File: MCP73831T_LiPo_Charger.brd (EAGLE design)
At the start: 12.7 x 24.1 mm, 10 parts, among them U4 MCP73831

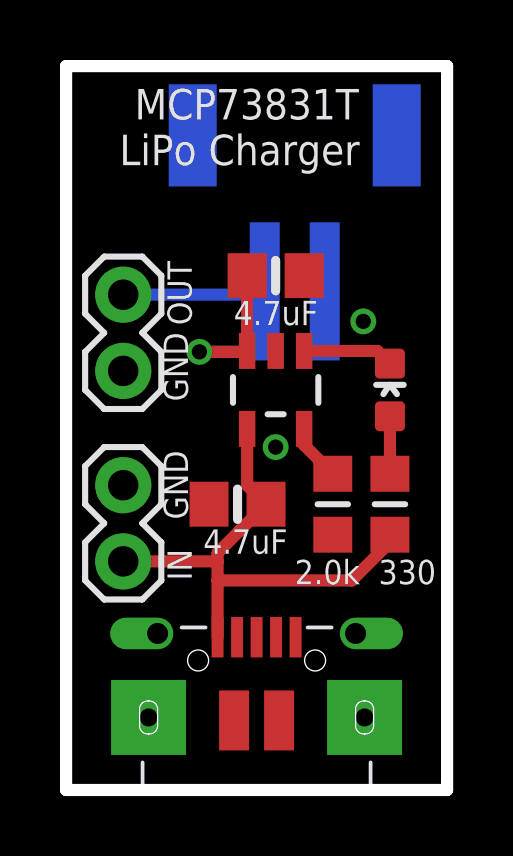
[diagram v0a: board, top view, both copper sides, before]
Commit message: modified microUSB port
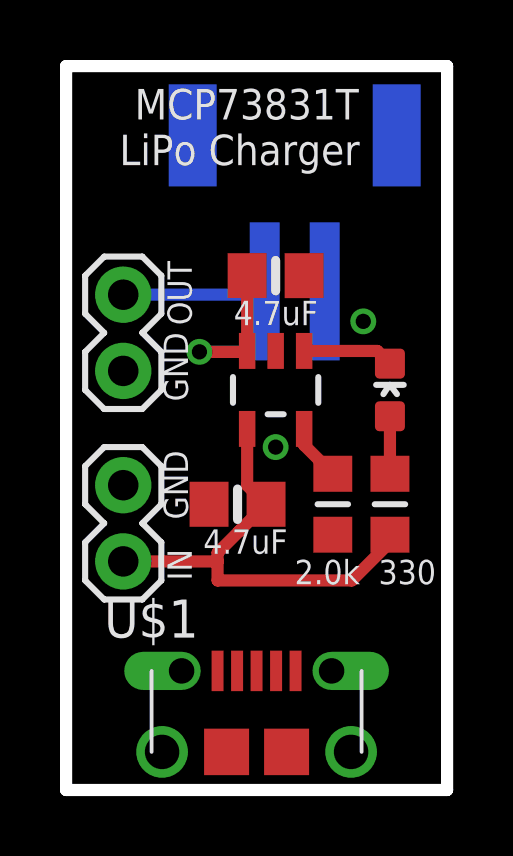
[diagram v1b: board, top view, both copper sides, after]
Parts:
- removed X1: (no value), microbuilder:4UCONN_20329
- added U$1: AMPHENOL_MICROUSB, sharkdunio:AMPHENOL_MICROUSB
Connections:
- net GND: now also U$1.2, U$1.3, U$1.4, U$1.5; no longer X1.BASE@1, X1.BASE@2, X1.GND, X1.SPRT@1, X1.SPRT@2, X1.SPRT@3, X1.SPRT@4
- net VIN: now also U$1.1; no longer X1.VBUS
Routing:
- net VIN: track 17.5 -> 15.6 mm
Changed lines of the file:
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@@
 <attribute name="VALUE" x="7.9375" y="13.5255" size="0.4064" layer="27" rot="R180"/>
 </element>
-<element name="X1" library="microbuilder" package="4UCONN_20329" value="" x="6.35" y="4.318" smashed="yes">
-<attribute name="VALUE" x="3.572" y="-2.092" size="0.4064" layer="27" ratio="10"/>
-</element>
+<element name="U$1" library="sharkdunio" package="AMPHENOL_MICROUSB" value="AMPHENOL_MICROUSB" x="6.35" y="1.27"/>
 </elements>
 <signals>
@@
 <contactref element="U4" pad="2"/>
 <contactref element="R8" pad="1"/>
-<contactref element="X1" pad="BASE@1"/>
-<contactref element="X1" pad="BASE@2"/>
-<contactref element="X1" pad="GND"/>
-<contactref element="X1" pad="SPRT@1"/>
-<contactref element="X1" pad="SPRT@2"/>
-<contactref element="X1" pad="SPRT@3"/>
-<contactref element="X1" pad="SPRT@4"/>
 <contactref element="JP1" pad="1"/>
 <contactref element="J1" pad="1"/>
@@
 <via x="6.985" y="11.43" extent="1-16" drill="0.508"/>
 <via x="9.906" y="15.621" extent="1-16" drill="0.508"/>
+<contactref element="U$1" pad="5"/>
+<contactref element="U$1" pad="4"/>
+<contactref element="U$1" pad="2"/>
+<contactref element="U$1" pad="3"/>
+<wire x1="8.62" y1="16.62" x2="7.935" y2="17.145" width="0" layer="19" extent="1-16"/>
+<wire x1="9.906" y1="15.621" x2="8.62" y2="16.62" width="0" layer="19" extent="16-16"/>
+<wire x1="6.985" y1="14.6351" x2="8.62" y2="16.62" width="0" layer="19" extent="1-16"/>
+<wire x1="6.985" y1="11.43" x2="6.985" y2="14.6351" width="0" layer="19" extent="1-1"/>
+<wire x1="4.765" y1="9.525" x2="6.985" y2="11.43" width="0" layer="19" extent="1-1"/>
+<wire x1="1.905" y1="10.16" x2="4.765" y2="9.525" width="0" layer="19" extent="1-1"/>
+<wire x1="8.89" y1="8.509" x2="6.985" y2="11.43" width="0" layer="19" extent="1-1"/>
+<wire x1="1.905" y1="13.97" x2="1.905" y2="10.16" width="0" layer="19" extent="1-1"/>
+<wire x1="7.65" y1="3.97" x2="8.89" y2="8.509" width="0" layer="19" extent="1-1"/>
+<wire x1="7" y1="3.97" x2="7.65" y2="3.97" width="0" layer="19" extent="1-1"/>
+<wire x1="6.35" y1="3.97" x2="7" y2="3.97" width="0" layer="19" extent="1-1"/>
+<wire x1="5.7" y1="3.97" x2="6.35" y2="3.97" width="0" layer="19" extent="1-1"/>
 </signal>
 <signal name="V_RAW">
@@
 <contactref element="R7" pad="1"/>
 <contactref element="C7" pad="1"/>
-<contactref element="X1" pad="VBUS"/>
 <contactref element="J1" pad="2"/>
 <wire x1="6.035" y1="12.0349" x2="6.035" y2="10.155" width="0.4064" layer="1"/>
@@
 <wire x1="5.7706" y1="8.62770625" x2="5.7706" y2="8.6306" width="0.4064" layer="1"/>
 <wire x1="5.7706" y1="8.6306" x2="6.665" y2="9.525" width="0.4064" layer="1"/>
-<wire x1="5.05" y1="6.985" x2="5.05" y2="5.093" width="0.4064" layer="1"/>
 <wire x1="5.05" y1="6.985" x2="5.05" y2="7.62" width="0.4064" layer="1"/>
 <wire x1="5.05" y1="7.62" x2="5.05" y2="7.90710625" width="0.4064" layer="1"/>
@@
 <wire x1="10.795" y1="8.255" x2="9.525" y2="6.985" width="0.4064" layer="1"/>
 <wire x1="9.525" y1="6.985" x2="5.05" y2="6.985" width="0.4064" layer="1"/>
+<contactref element="U$1" pad="1"/>
+<wire x1="5.05" y1="3.97" x2="5.05" y2="6.985" width="0" layer="19" extent="1-1"/>
 </signal>
 </signals>

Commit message: modified microusb port and lipo schematic
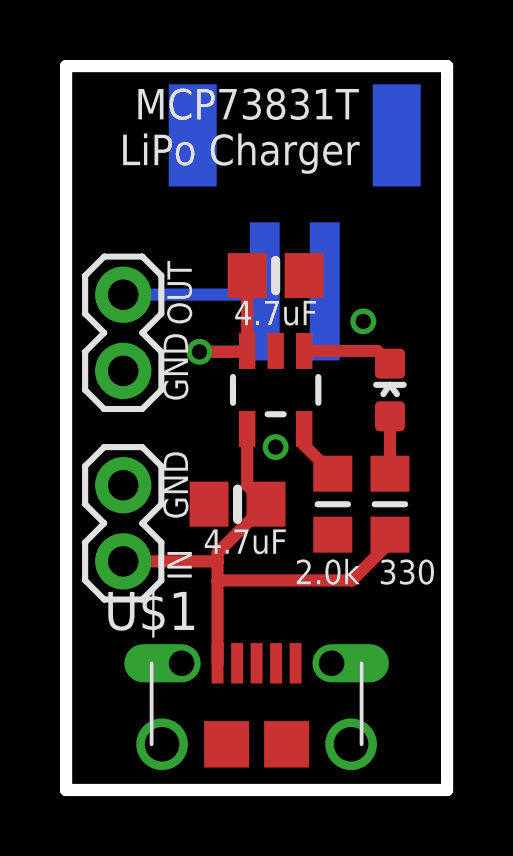
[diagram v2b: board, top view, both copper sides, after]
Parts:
- moved U$1 0.25 mm to (6.35, 1.52)
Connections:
- net GND: now also U$1.10, U$1.11, U$1.6, U$1.7, U$1.8, U$1.9; no longer U$1.2, U$1.3, U$1.4
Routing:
- net VIN: track 15.6 -> 18.4 mm
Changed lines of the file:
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@@
 <attribute name="VALUE" x="7.9375" y="13.5255" size="0.4064" layer="27" rot="R180"/>
 </element>
-<element name="U$1" library="sharkdunio" package="AMPHENOL_MICROUSB" value="AMPHENOL_MICROUSB" x="6.35" y="1.27"/>
+<element name="U$1" library="sharkdunio" package="AMPHENOL_MICROUSB" value="AMPHENOL_MICROUSB" x="6.35" y="1.524"/>
 </elements>
 <signals>
@@
 <via x="6.985" y="11.43" extent="1-16" drill="0.508"/>
 <via x="9.906" y="15.621" extent="1-16" drill="0.508"/>
+<contactref element="U$1" pad="6"/>
+<contactref element="U$1" pad="7"/>
+<contactref element="U$1" pad="8"/>
+<contactref element="U$1" pad="9"/>
+<contactref element="U$1" pad="10"/>
+<contactref element="U$1" pad="11"/>
 <contactref element="U$1" pad="5"/>
-<contactref element="U$1" pad="4"/>
-<contactref element="U$1" pad="2"/>
-<contactref element="U$1" pad="3"/>
-<wire x1="8.62" y1="16.62" x2="7.935" y2="17.145" width="0" layer="19" extent="1-16"/>
-<wire x1="9.906" y1="15.621" x2="8.62" y2="16.62" width="0" layer="19" extent="16-16"/>
-<wire x1="6.985" y1="14.6351" x2="8.62" y2="16.62" width="0" layer="19" extent="1-16"/>
-<wire x1="6.985" y1="11.43" x2="6.985" y2="14.6351" width="0" layer="19" extent="1-1"/>
-<wire x1="4.765" y1="9.525" x2="6.985" y2="11.43" width="0" layer="19" extent="1-1"/>
-<wire x1="1.905" y1="10.16" x2="4.765" y2="9.525" width="0" layer="19" extent="1-1"/>
-<wire x1="8.89" y1="8.509" x2="6.985" y2="11.43" width="0" layer="19" extent="1-1"/>
-<wire x1="1.905" y1="13.97" x2="1.905" y2="10.16" width="0" layer="19" extent="1-1"/>
-<wire x1="7.65" y1="3.97" x2="8.89" y2="8.509" width="0" layer="19" extent="1-1"/>
-<wire x1="7" y1="3.97" x2="7.65" y2="3.97" width="0" layer="19" extent="1-1"/>
-<wire x1="6.35" y1="3.97" x2="7" y2="3.97" width="0" layer="19" extent="1-1"/>
-<wire x1="5.7" y1="3.97" x2="6.35" y2="3.97" width="0" layer="19" extent="1-1"/>
 </signal>
 <signal name="V_RAW">
@@
 <wire x1="10.795" y1="8.509" x2="10.795" y2="8.255" width="0.4064" layer="1"/>
 <wire x1="10.795" y1="8.255" x2="9.525" y2="6.985" width="0.4064" layer="1"/>
-<wire x1="9.525" y1="6.985" x2="5.05" y2="6.985" width="0.4064" layer="1"/>
+<wire x1="5.08" y1="6.985" x2="9.525" y2="6.985" width="0.4064" layer="1"/>
 <contactref element="U$1" pad="1"/>
-<wire x1="5.05" y1="3.97" x2="5.05" y2="6.985" width="0" layer="19" extent="1-1"/>
+<wire x1="5.08" y1="6.985" x2="5.05" y2="6.985" width="0.4064" layer="1"/>
+<wire x1="5.05" y1="4.224" x2="5.05" y2="6.955" width="0.4064" layer="1"/>
+<wire x1="5.05" y1="6.955" x2="5.08" y2="6.985" width="0.4064" layer="1"/>
 </signal>
 </signals>
